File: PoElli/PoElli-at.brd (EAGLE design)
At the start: 100 x 80 mm, 130 parts, among them J1 DF12-ELLI-HEADER-TOP, J3 M022.54MM_SCREWTERM, J4 M022.54MM_SCREWTERM, Q1 SI1307DL, Q2 FDV301N, Q3 FDMC2674, T1 Coilcraft 230NL, T2 FLYBACK750311689, U1 ENC624J600-I/PT, U2 NCP1117, U3 FST3257, U4 LT3748, U5 TPS2378, X1 POE-TP-RJ45-MOLEX, Y1 25MHz

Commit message: Change to ENC424J600 & cleanups in PoElli
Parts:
- removed U1: ENC624J600-I/PT, ELL-i-DigitalIC:QFP50P1200X1200X120-64N
- added U6: ENC424J600, ELL-i-DigitalIC:TQFP44-0.8MM
- D11, D6: device ELL-i-DIscreteSemi:SOD323 -> ELL-i-DIscreteSemi:SOD-323
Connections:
- net ENC-3V3: now also U6.12, U6.15, U6.18, U6.4, U6.44; no longer U1.21, U1.22, U1.25, U1.28, U1.4, U1.47, U1.64
- net ETH_INT: now also U6.24; no longer U1.34
- net ETH_MISO: now also U6.35; no longer U1.50
- net ETH_MOSI: now also U6.36; no longer U1.51
- net ETH_SCK: now also U6.37; no longer U1.52
- net ETH_SS: now also U6.34; no longer U1.49
- net GNDA: now also U6.1, U6.13, U6.14, U6.19, U6.22, U6.25, U6.26, U6.27, U6.28, U6.29, U6.30, U6.31, U6.32, U6.33, U6.38, U6.39, U6.40, U6.41, U6.42, U6.5, U6.6, U6.7, U6.8; no longer U1.1, U1.10, U1.11, U1.12, U1.13, U1.17, U1.18, U1.19, U1.20, U1.23, U1.24, U1.29, U1.32, U1.35, U1.36, U1.37, U1.38, U1.39, U1.40, U1.41, U1.42, U1.43, U1.44, U1.45, U1.46, U1.48, U1.5, U1.53, U1.54, U1.55, U1.56, U1.57, U1.58, U1.59, U1.6, U1.60, U1.61, U1.62, U1.7, U1.8, U1.9
- net N$37: now also U6.2; no longer U1.2
- net N$39: now also U6.17; no longer U1.27
- net N$41: now also U6.9; no longer U1.14
- net N$42: now also U6.10; no longer U1.15
- net N$45: now also U6.11; no longer U1.16
- net N$46: now also U6.43; no longer U1.63
- net N$47: now also U6.3; no longer U1.3
- net N$59: now also U6.16; no longer U1.26
- net TPOUT+: now also R13.1, U6.20; no longer R12.1, U1.31
- net TPOUT-: now also R12.1, U6.21; no longer R13.1, U1.30

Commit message: Initial layout for PoElli
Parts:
- removed XXR35XX: 47k, ELL-i-Passives:R0805
- added R39: 47k, ELL-i-Passives:R0805
- SV1: value RASPBERRYPI-GPIOPTH -> RASPBERRY-SHIELD; device SparkFun-Boards:2X13-SHROUDED -> ELL-i-Boards:RASPBERRYPI-SHIELD-FULLSIZE
- TP1, TP5, TP6, TP7, TP8, TP9: value TEST_POINT-5000 -> (none)
- TP10: value TEST_POINT-BARE -> (none)
- TP2, TP3, TP4: value TEST_POINT-5021 -> (none)
- X1: value POE-TP-RJ45-MOLEX -> RJ45
- moved U6 124.8 mm to (21.0, 73.5)
- moved C13 101.0 mm to (8.63, 13.2)
- moved R27 97.6 mm to (81.2, 21.3)
- moved C28 95.5 mm to (63.2, 36.2)
- moved C33 90.5 mm to (76.0, 21.0)
- moved R16 88.1 mm to (15.2, 31.6)
- moved C21 88.0 mm to (13.2, 26.4)
- moved J1 84.2 mm to (4.25, 28.9), turned to 90 degrees
- moved R6 84.0 mm to (11.2, 75.2)
- moved TP5 83.7 mm to (2.82, 26.0)
- moved R37 78.9 mm to (18.4, 38.6)
- moved C38 78.2 mm to (36.0, 7.00)
- moved TP9 77.8 mm to (9.82, 77.3)
- moved D4 75.1 mm to (20.9, 6.61), turned to 180 degrees
- moved D5 73.8 mm to (28.5, 28.9)
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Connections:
- net ETH_INT: now also R39.2; no longer XXR35XX.2
- net TX+: now also R39.1; no longer XXR35XX.1

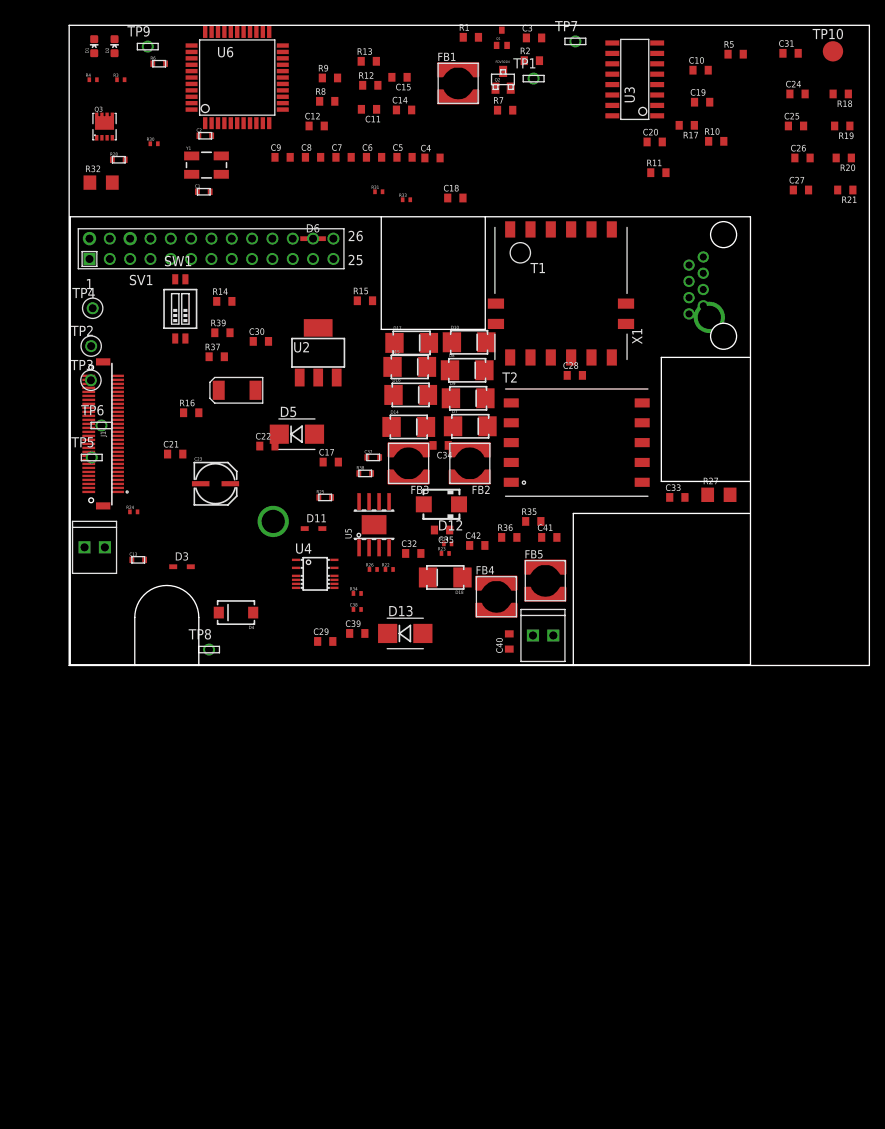
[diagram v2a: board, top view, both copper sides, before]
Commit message: Minor mods to PoElli initial layout
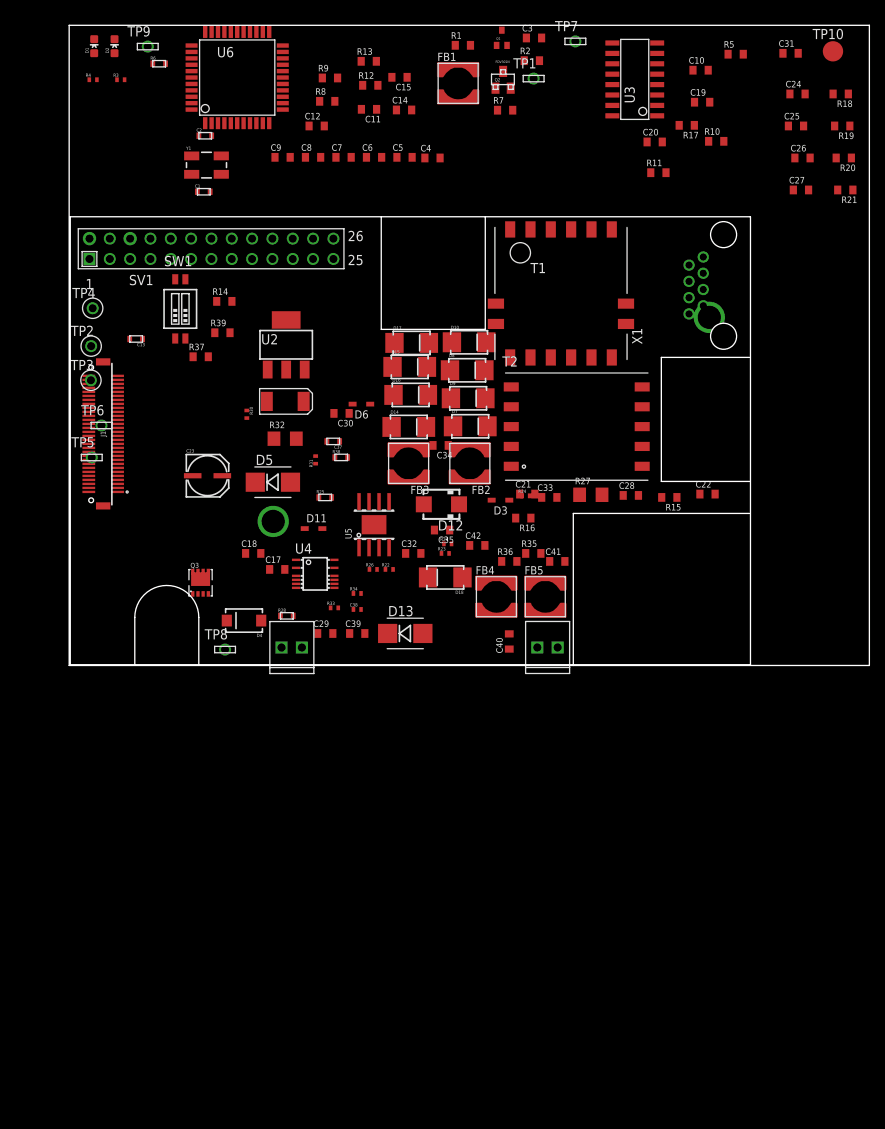
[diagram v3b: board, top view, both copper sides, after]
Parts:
- moved R28 60.7 mm to (27.2, 6.20)
- moved Q3 58.2 mm to (16.4, 10.3)
- moved C22 55.3 mm to (79.8, 21.4)
- moved R33 51.8 mm to (33.1, 7.20)
- moved C18 51.1 mm to (23.0, 14.0)
- moved R24 49.0 mm to (57.1, 21.2)
- moved R15 45.3 mm to (75.0, 21.0), turned to 180 degrees
- moved C21 44.3 mm to (57.2, 21.4)
- moved R16 43.5 mm to (56.8, 18.4), turned to 180 degrees
- moved D3 40.7 mm to (53.9, 20.7), turned to 180 degrees
- moved R32 39.4 mm to (27.0, 28.3)
- moved R30 35.7 mm to (22.2, 31.4), turned to 270 degrees
- moved R31 34.4 mm to (30.8, 25.7), turned to 90 degrees
- moved J3 29.9 mm to (29.1, 2.24), turned to 180 degrees
- moved C13 27.6 mm to (8.37, 40.8), turned to 180 degrees
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
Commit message: Review changes to PoElli-at
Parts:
- removed D1: (no value), SparkFun-LED:LED-0603
- removed D2: GREEN, SparkFun-LED:LED-0603
- removed R11: 0R, ELL-i-Passives:R0805
- removed TP10: (no value), ELL-i-Passives:TP_BARE
- added C36: 47p, ELL-i-Passives:C0402
- added C43, C44, C45, C46, C47: 22uF, ELL-i-Passives:C0805
- added C48: 1nF, ELL-i-Passives:C1206
- added D19: B2100, ELL-i-DIscreteSemi:DIODE-B2100
- added Q4: IRFL4310, ELL-i-DIscreteSemi:SOT223
- added SJ1: CLOSED, SparkFun-Passives:SJ_2S
- added SJ2, SJ3: OPEN, SparkFun-Passives:SJ_2S-NO
- C1, C2, C37: device ELL-i-Passives:C0603 -> ELL-i-Passives:C0402
- C10, C11, C12, C14, C15, C17, C18, C19, C20, C3, C39, C4, C5, C6, C7, C8, C9: device ELL-i-Passives:C0805 -> ELL-i-Passives:C0402
- C16: value 47u -> 47uF; device ELL-i-Passives:CT6032 -> ELL-i-Passives:CT3216
- C22, C24, C25, C26, C27, C34, C40, C42: device ELL-i-Passives:C0805 -> ELL-i-Passives:C0603
- C23: value (none) -> 220uF; device ELL-i-Passives:CPOL_PANASONIC_C -> ELL-i-Passives:CPOL_PANASONIC_E
- C28: value 33nF -> 1nF; device ELL-i-Passives:C0805 -> ELL-i-Passives:C1206
- C31: device ELL-i-Passives:C0805 -> ELL-i-Passives:C1210
- C32: device ELL-i-Passives:C0805 -> ELL-i-Passives:CT3216
- D12: device ell-i:SMA -> ELL-i-DIscreteSemi:SMA
- D13: value TBD 18V -> 18V; device SparkFun-DiscreteSemi:SMB-DIODE -> ELL-i-DIscreteSemi:SOD-123FL
- D5: value 5.1V TBD -> 5.6V TBD; device SparkFun-DiscreteSemi:SMB-DIODE -> ELL-i-DIscreteSemi:SOD-123FL
- FB1: device ELL-i-Passives:COILCRAFT-MSS5121 -> ELL-i-Passives:FB0402
- FB2, FB3, FB4, FB5: device ELL-i-Passives:COILCRAFT-MSS5121 -> ELL-i-Passives:FB1206
- J3, J4: value M022.54MM_SCREWTERM -> M022.54MM
- R1, R12, R13, R14, R17, R2, R7, R8, R9: device ELL-i-Passives:R0805 -> ELL-i-Passives:R0402
- R10: value 0R -> 100; device ELL-i-Passives:R0805 -> ELL-i-Passives:R0603
- R15, R18, R19, R20, R21, R35, R36, R5: device ELL-i-Passives:R0805 -> ELL-i-Passives:R0603
- R16: device ELL-i-Passives:R0805 -> ELL-i-Passives:R1206
- R22, R23, R24, R26, R30, R31, R33, R34: device ELL-i-Passives:R0402 -> ELL-i-Passives:R0603
- R27, R32: device ELL-i-Passives:R1206 -> ELL-i-Passives:R0805
- R29: device ELL-i-Passives:R0402 -> ELL-i-Passives:R0805
- R3, R4: value 180 -> 330
- R38: value 0R NP -> OPEN; device ELL-i-Passives:R0603 -> SparkFun-Passives:SJ_2S-NO
- R6: device ELL-i-Passives:R0603 -> ELL-i-Passives:R0402
- U2: device ell-i:SOT223 -> ELL-i-PowerIC:SOT223
- X1: value RJ45 -> XMK-8788K5-BX1X; device ELL-i-Connectors:MOLEX-43860-0001 -> ELL-i-Connectors:XMK-8788K5-BX1X
- Y1: value 25MHz -> 25 MHz; device SparkFun-FreqCtrl:CRYSTAL-SMD-5X3 -> SparkFun-FreqCtrl:CRYSTAL-SMD-3225-GND
- moved R10 51.1 mm to (54.0, 22.0)
- moved J3 24.0 mm to (5.08, 2.24)
- moved D8 15.3 mm to (65.0, 38.0), flipped to the bottom
- moved D9 15.2 mm to (65.0, 34.0), flipped to the bottom
- moved D10 15.1 mm to (65.0, 42.4), flipped to the bottom
- moved D17 15.1 mm to (57.8, 42.3), flipped to the bottom
- moved D15 15.0 mm to (57.6, 38.3), flipped to the bottom
- moved D14 15.0 mm to (57.4, 29.8), flipped to the bottom
- moved D16 15.0 mm to (57.7, 33.8), flipped to the bottom
- moved D7 14.9 mm to (65.0, 30.0), flipped to the bottom
- moved Y1 10.3 mm to (7.00, 64.0)
- moved X1 9.42 mm to (72.7, 50.0)
- moved TP8 2.83 mm to (17.5, 3.99)
- moved J1 1.20 mm to (5.00, 28.0)
- moved T1 0.08 mm to (61.5, 46.5), turned to 180 degrees
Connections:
- removed net 3.3V: SV1.1, SV1.17
- removed net GND: C28.1, R27.2
- removed net VCC(IO): J1.2
- new net N$21: D19.C, J3.P1
- new net N$34: C21.2, R10.2
- new net N$35: J1.2, SJ3.1
- net +3V3: now also C16.A, SJ1.2, SJ3.2; no longer C16.P$1, R10.2
- net +5V0: now also SJ2.2; no longer R11.2
- net 5V: now also C43.1, C44.1, C45.1, C46.1, C47.1
- net GNDA: now also C16.C, C43.2, C44.2, C45.2, C46.2, C47.2, C48.2, X1.10, X1.12, Y1.2, Y1.4; no longer C16.P$2, D1.C, D2.C
- net N$10: now also Q4.2, Q4.4
- net N$26: now also C36.1
- net N$33: now also R10.1; no longer C21.2
- net N$36: now also X1.9; no longer D1.A
- net N$38: now also X1.11; no longer D2.A
- net N$43: now also SJ1.1, SJ2.1; no longer R10.1, R11.1
- net N$9: now also Q4.1
- net RTN: now also C28.1, C32.C, C36.2, C48.1, Q4.3, R27.2, SV1.1, SV1.17, X1.SGND1, X1.SGND2, X1.SGND3, X1.SGND4; no longer C32.2
- net SGND: no longer TP10.P$1
- net VDD: now also C32.A, D19.A; no longer C32.1, J3.P1

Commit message: Mechanical design
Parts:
- added JP1: XMK-8788K5-BX1X, ELL-i-Connectors:XMK-8788K5-BX1X
- added X2, X3, X4: M-BOLT-2, ELL-i-Connectors:M2-1
- X1: value XMK-8788K5-BX1X -> M-BOLT-2; device ELL-i-Connectors:XMK-8788K5-BX1X -> ELL-i-Connectors:M2-1
- moved X1 67.9 mm to (5.50, 40.5), turned to 0 degrees
- moved TP5 44.6 mm to (33.8, 58.0)
- moved TP6 37.5 mm to (29.0, 58.0)
- moved TP3 28.6 mm to (19.7, 58.6)
- moved TP2 21.5 mm to (10.8, 59.9)
- moved TP4 14.0 mm to (3.94, 58.6)
- moved R23 6.40 mm to (43.0, 19.0)
- moved C13 6.40 mm to (3.37, 44.8)
- moved D19 5.39 mm to (19.0, 22.0)
- moved C23 5.39 mm to (15.2, 28.9)
- moved SJ3 5.10 mm to (2.00, 16.0), turned to 180 degrees
- moved R29 5.00 mm to (42.3, 15.2)
- moved C47 4.47 mm to (31.0, 3.00)
- moved Q3 4.47 mm to (20.4, 12.3)
- moved TP8 4.00 mm to (17.5, 7.99)
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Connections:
- net 5V: now also X1.1
- net GNDA: now also JP1.10, JP1.12, X2.1; no longer X1.10, X1.12
- net N$1: now also JP1.2; no longer X1.2
- net N$2: now also JP1.1; no longer X1.1
- net N$3: now also JP1.3; no longer X1.3
- net N$36: now also JP1.9; no longer X1.9
- net N$38: now also JP1.11; no longer X1.11
- net N$4: now also JP1.6; no longer X1.6
- net POE_B+: now also JP1.4, JP1.5; no longer X1.4, X1.5
- net POE_B-: now also JP1.7, JP1.8; no longer X1.7, X1.8
- net RTN: now also JP1.SGND1, JP1.SGND2, JP1.SGND3, JP1.SGND4, X4.1; no longer X1.SGND1, X1.SGND2, X1.SGND3, X1.SGND4
- net VDD: now also X3.1

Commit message: Work on PoElli-at
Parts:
- moved D6 15.7 mm to (50.5, 25.7)
- moved D13 11.4 mm to (35.0, 13.0), turned to 270 degrees
- moved FB3 11.3 mm to (39.8, 38.4), turned to 270 degrees
- moved R29 11.2 mm to (40.3, 26.2)
- moved D12 10.4 mm to (43.5, 32.1)
- moved C34 9.22 mm to (44.4, 38.5)
- moved FB2 9.06 mm to (49.1, 36.2)
- moved R38 8.49 mm to (28.0, 20.0)
- moved C42 6.40 mm to (50.0, 21.0)
- moved C35 6.32 mm to (44.6, 24.9)
- moved R36 4.47 mm to (53.0, 17.0), turned to 180 degrees
- moved R35 4.00 mm to (54.0, 14.0)
- moved C30 3.61 mm to (36.0, 28.5)
- moved R23 3.61 mm to (46.0, 21.0)
- moved C41 3.16 mm to (58.0, 14.0)
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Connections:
- net N$21: now also X3.1
- net VDD: no longer X3.1
